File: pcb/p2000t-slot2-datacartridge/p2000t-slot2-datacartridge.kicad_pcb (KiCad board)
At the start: 4 copper layers, 80 x 100 mm, 27 parts, among them J1 P2000T Port 2, U1 74HC04, U11 CY62256-70PC, U13 74HC173, U14 ZIF, U15 74HC02, U3 74HC138, U4 74HC21, U5 SST39SF040, U6 74HC02, U8 74HC273, U9 74HC273

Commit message: Improving lay-out board
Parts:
- removed U15: 74HC02, Package_DIP:DIP-14_W7.62mm_Socket
- added U9: 74HC173, Package_DIP:DIP-16_W7.62mm_Socket, B.Cu at (53.7, 93.1)
- moved C6 5.24 mm to (48.7, 89.3), turned to 0 degrees
- moved C10 5.00 mm to (92.8, 112.4), turned to 0 degrees
- renumbered U6 to U1, U14 to U10, U1 to U2, U8 to U5, U9 to U6, U13 to U7, U5 to U8
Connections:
- U1 pad 10: unconnected-(U6-Pad10) -> Net-(U9-Pad7)
- U1 pad 8: VCC -> SO6
- U1 pad 9: VCC -> ~{WR}
- U2 pad 12: unconnected-(U1-Pad12) -> (no net)
- U2 pad 13: VCC -> (no net)
- U3 pad 9: unconnected-(U3-Pad9) -> SO6
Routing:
- net GND: track 109.2 -> 538.8 mm, vias 8 -> 1
- net VCC: track 87.1 -> 381.4 mm, vias 5 -> 3
- net D1: track 183.2 -> 288.5 mm, vias 1 -> 4
- net SO5: track 132.2 -> 59.4 mm, vias 1 -> 0
- net CA16: track 91.5 -> 160.4 mm, vias 0 -> 3
- net D3: track 148.5 -> 204.1 mm, vias 0 -> 3
- net CA17: track 84.6 -> 133.1 mm, vias 0 -> 2
- net D5: track 138.6 -> 176.8 mm, vias 1 -> 0
- net D0: track 184.2 -> 221.3 mm, vias 1 -> 3
- net CA0: track 115.4 -> 149.5 mm, vias 0 -> 2
- net Net-(U9-Pad7): track 0.00 -> 30.4 mm, vias 0 -> 1
- net Net-(U3-Pad6): track 35.3 -> 64.2 mm, vias 0 -> 2
- net ~{RES}: track 111.1 -> 138.9 mm, vias 1 -> 3
- net D2: track 201.4 -> 227.1 mm, vias 1 -> 2
- net SO6: track 0.00 -> 24.2 mm
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- removed copper zone on F.Cu, net GND
- removed copper zone on B.Cu, net VCC
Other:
- copper layers 4 -> 2
- board text added: "P2000T DATACARTRIDGE rev1"
- board text added: "www.philips-p2000t.nl"

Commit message: Initial commit rev2 and implementing LEDs in firmware flasher
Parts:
- moved U3 50.0 mm to (53.3, 92.7)
- moved U9 49.5 mm to (97.8, 115.6)
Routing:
- net GND: track 538.8 -> 69.5 mm, vias 1 -> 0
- net D1: track 288.5 -> 0.00 mm, vias 4 -> 0
- net D2: track 227.1 -> 0.00 mm, vias 2 -> 0
- net D0: track 221.3 -> 0.00 mm, vias 3 -> 0
- net D3: track 204.1 -> 0.00 mm, vias 3 -> 0
- net D5: track 176.8 -> 0.00 mm
- net CA18: track 161.2 -> 0.00 mm, vias 1 -> 0
- net CA16: track 160.4 -> 0.00 mm, vias 3 -> 0
- net ~{WR}: track 158.0 -> 0.00 mm, vias 3 -> 0
- net CA0: track 149.5 -> 0.00 mm, vias 2 -> 0
- net D7: track 140.5 -> 0.00 mm, vias 4 -> 0
- net D4: track 139.6 -> 0.00 mm, vias 1 -> 0
- net ~{RES}: track 138.9 -> 0.00 mm, vias 3 -> 0
- net D6: track 137.2 -> 0.00 mm, vias 3 -> 0
- net CA17: track 133.1 -> 0.00 mm, vias 2 -> 0
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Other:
- outline, holes or cut-outs redrawn
- board text added: "P2000T DATACARTRIDGE rev2 @ 2023/10/28"
- board text removed: "P2000T DATACARTRIDGE rev1"

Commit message: Fixing incorrect RES line
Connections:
- U2 pad 10: unconnected-(U2-Pad10) -> Net-(U2-Pad10)
- U2 pad 11: VCC -> ~{RES}
- U9 pad 15: ~{RES} -> Net-(U2-Pad10)
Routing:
- net GND: track 69.5 -> 487.1 mm
- net D0: track 0.00 -> 252.7 mm, vias 0 -> 3
- net D2: track 0.00 -> 228.9 mm, vias 0 -> 3
- net D1: track 0.00 -> 199.7 mm, vias 0 -> 2
- net CA18: track 0.00 -> 195.9 mm, vias 0 -> 2
- net D3: track 0.00 -> 195.0 mm, vias 0 -> 1
- net D4: track 0.00 -> 168.8 mm, vias 0 -> 2
- net D5: track 0.00 -> 164.3 mm, vias 0 -> 2
- net ~{WR}: track 0.00 -> 160.6 mm, vias 0 -> 4
- net D7: track 0.00 -> 148.8 mm, vias 0 -> 1
- net CA16: track 0.00 -> 147.2 mm, vias 0 -> 2
- net CA17: track 0.00 -> 144.2 mm, vias 0 -> 2
- net D6: track 0.00 -> 143.1 mm, vias 0 -> 2
- net ~{RES}: track 0.00 -> 127.6 mm, vias 0 -> 2
- net ~{RD}: track 0.00 -> 119.6 mm, vias 0 -> 3
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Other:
- board text added: "P2000T DATACARTRIDGE rev2 @ 2023/10/29"
- board text removed: "P2000T DATACARTRIDGE rev2 @ 2023/10/28"

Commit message: Building rev2 of the data cartridge
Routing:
- net ~{RD}: track 119.6 -> 108.9 mm
- net CA0: track 115.1 -> 123.9 mm, vias 3 -> 2
- net ~{RES}: track 127.6 -> 125.1 mm
- net CA15: track 71.6 -> 69.7 mm
- net Net-(R1-Pad1): track 72.6 -> 71.0 mm
- net CA12: track 109.1 -> 108.0 mm
- net D1: track 199.7 -> 198.6 mm
- net CA18: track 195.9 -> 194.8 mm
- net CA5: track 66.6 -> 65.7 mm
- net A5: track 35.7 -> 34.9 mm
- net CA1: track 111.0 -> 111.8 mm
- net ~{WR}: track 160.6 -> 159.9 mm
- net D6: track 143.1 -> 143.8 mm
- net CA11: track 99.6 -> 100.4 mm
- net D4: track 168.8 -> 168.0 mm
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
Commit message: Initial commit revision
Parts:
- U11: footprint Package_DIP:DIP-28_W15.24mm_Socket -> Package_DIP:DIP-28_W15.24mm
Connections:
- J1 pad 11b: M1 -> unconnected-(J1-Pin_11b-Pad11b)
- J1 pad 7b: unconnected-(J1-Pad7b) -> A3
- U2 pad 12: (no net) -> unconnected-(U2-Pad12)
- U2 pad 13: (no net) -> GND
- U2 pad 5: M1 -> A3
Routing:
- net GND: track 487.1 -> 0.00 mm
- net VCC: track 392.2 -> 0.00 mm
- net D0: track 253.2 -> 0.00 mm, vias 3 -> 0
- net D2: track 229.3 -> 0.00 mm, vias 3 -> 0
- net D1: track 198.6 -> 0.00 mm, vias 2 -> 0
- net D3: track 194.9 -> 0.00 mm, vias 1 -> 0
- net CA18: track 194.8 -> 0.00 mm, vias 2 -> 0
- net D4: track 168.0 -> 0.00 mm, vias 2 -> 0
- net D5: track 164.3 -> 0.00 mm, vias 2 -> 0
- net ~{WR}: track 159.9 -> 0.00 mm, vias 4 -> 0
- net D7: track 148.7 -> 0.00 mm, vias 1 -> 0
- net CA16: track 147.6 -> 0.00 mm, vias 2 -> 0
- net CA17: track 144.4 -> 0.00 mm, vias 2 -> 0
- net D6: track 143.8 -> 0.00 mm, vias 2 -> 0
- net ~{RES}: track 125.1 -> 0.00 mm, vias 2 -> 0
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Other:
- board text added: "P2000T DATACARTRIDGE rev3 @ 2023/10/29"
- board text removed: "P2000T DATACARTRIDGE rev2 @ 2023/10/29"

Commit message: Interim commit
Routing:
- net GND: track 0.00 -> 594.9 mm, vias 0 -> 2
- net VCC: track 0.00 -> 361.6 mm

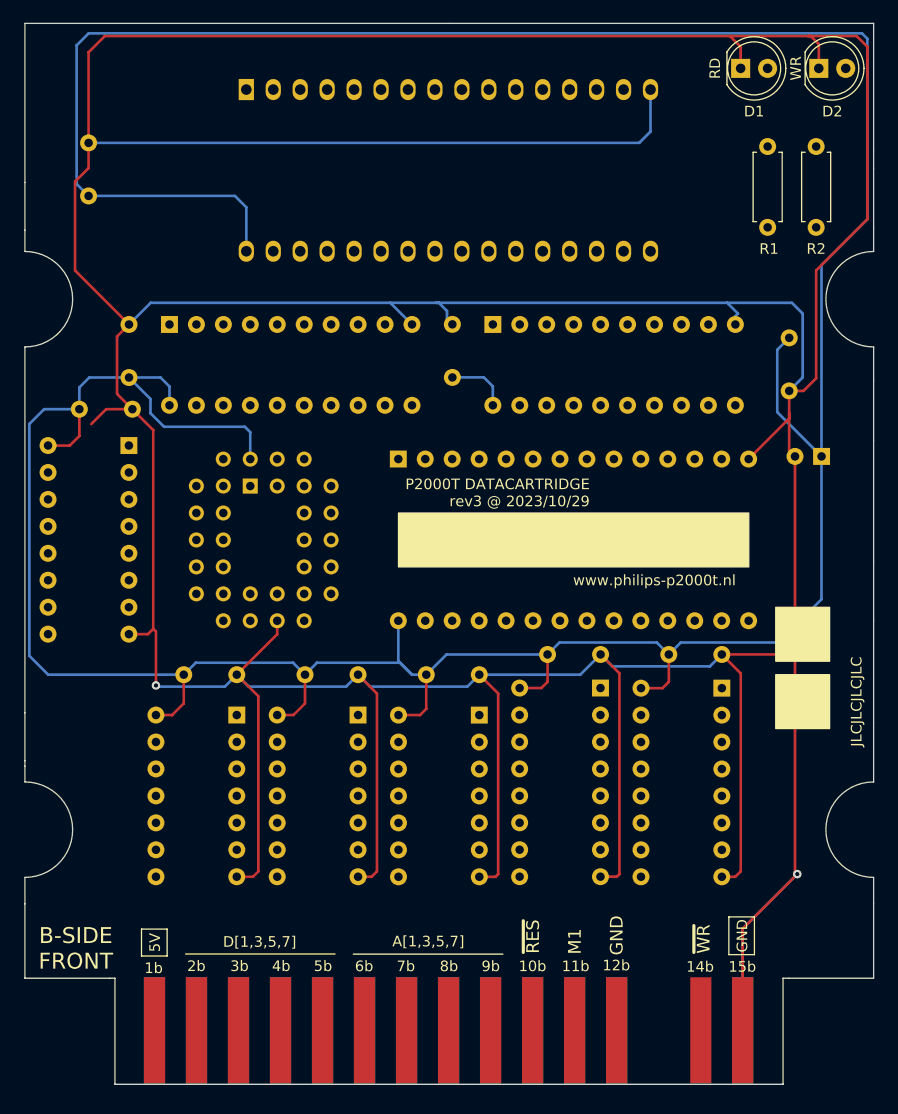
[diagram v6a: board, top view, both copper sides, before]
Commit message: Rerouting
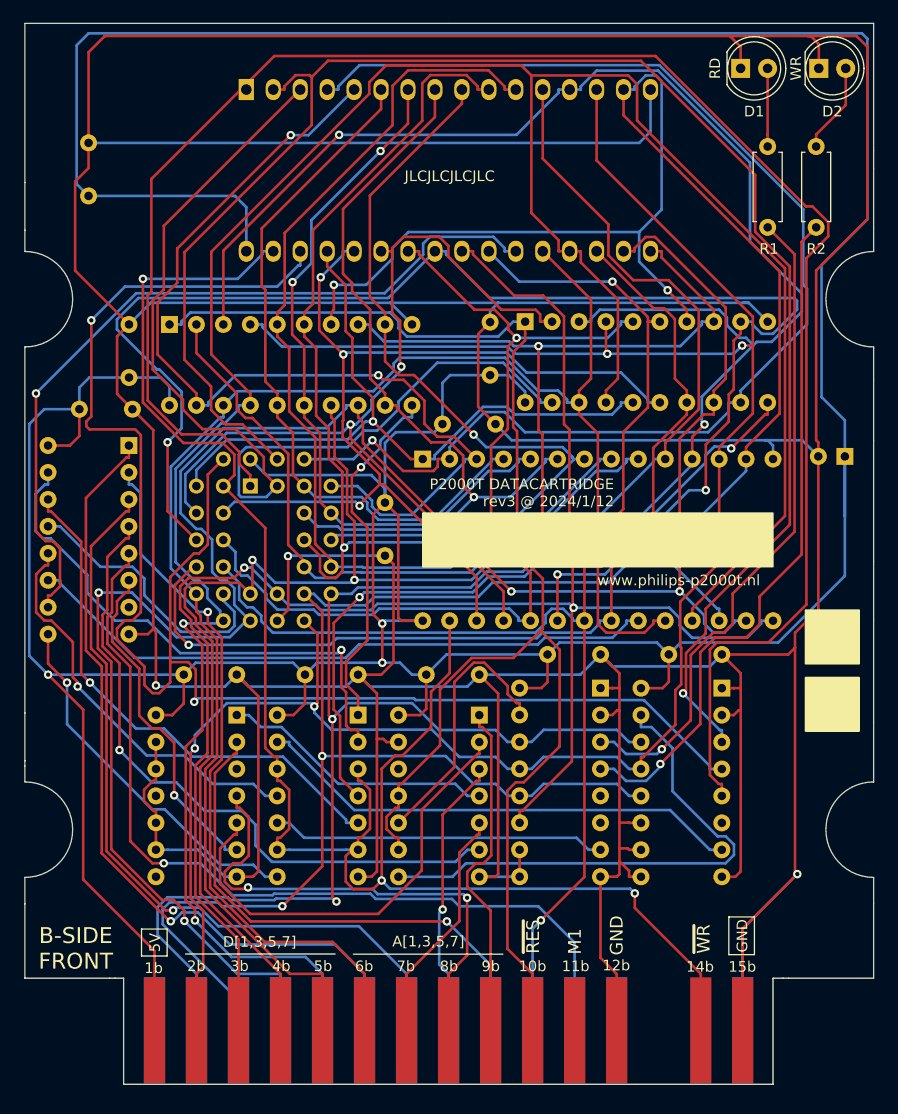
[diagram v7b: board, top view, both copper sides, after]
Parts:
- added C12: 0.1uF, Capacitor_THT:C_Disc_D5.0mm_W2.5mm_P5.00mm, B.Cu at (77.5, 98.1)
- U11: footprint Package_DIP:DIP-28_W15.24mm -> Package_DIP:DIP-28_W15.24mm_Socket
- moved C8 33.7 mm to (82.9, 90.7), turned to 0 degrees
- moved C7 3.56 mm to (87.4, 86.1)
- moved U5 3.05 mm to (90.7, 81.0)
- moved U11 2.30 mm to (81.0, 94.0)
- moved C11 2.20 mm to (120.8, 93.7)
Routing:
- net D0: track 0.00 -> 253.6 mm, vias 0 -> 4
- net D2: track 0.00 -> 246.2 mm, vias 0 -> 4
- net D6: track 0.00 -> 239.8 mm, vias 0 -> 2
- net D1: track 0.00 -> 211.4 mm, vias 0 -> 4
- net D3: track 0.00 -> 200.1 mm, vias 0 -> 3
- net D4: track 0.00 -> 195.4 mm, vias 0 -> 4
- net CA18: track 0.00 -> 173.1 mm
- net ~{WR}: track 0.00 -> 169.1 mm, vias 0 -> 3
- net CA16: track 0.00 -> 157.4 mm, vias 0 -> 1
- net D5: track 0.00 -> 157.4 mm, vias 0 -> 4
- net D7: track 0.00 -> 153.0 mm
- net CA17: track 0.00 -> 150.0 mm, vias 0 -> 2
- net CA11: track 0.00 -> 141.9 mm, vias 0 -> 3
- net ~{RES}: track 0.00 -> 138.7 mm
- net ~{RD}: track 0.00 -> 122.3 mm, vias 0 -> 1
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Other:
- outline, holes or cut-outs redrawn
- board text added: "P2000T DATACARTRIDGE rev3 @ 2024/1/12"
- board text removed: "P2000T DATACARTRIDGE rev3 @ 2023/10/29"

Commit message: Fixing bug in PCB
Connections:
- U2 pad 5: A3 -> GND
- U2 pad 6: Net-(U3-E1) -> unconnected-(U2-Pad6)
- U3 pad 4: Net-(U3-E1) -> A3
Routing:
- net Net-(U3-E1): track 62.8 -> 0.00 mm, vias 1 -> 0
- net A3: track 22.5 -> 69.7 mm, vias 0 -> 4
- net GND: track 696.1 -> 714.8 mm, vias 3 -> 5
- net A6: track 49.8 -> 50.5 mm
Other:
- board text added: "P2000T DATACARTRIDGE rev4 @ 2024/1/21"
- board text removed: "P2000T DATACARTRIDGE rev3 @ 2024/1/12"
